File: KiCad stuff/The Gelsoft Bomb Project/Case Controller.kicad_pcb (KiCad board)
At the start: 2 copper layers, 53.3 x 55.9 mm, 9 parts, among them J1 ISP, J2 Module Connector, J3 Battery, U1 L7805, U2 ATtiny24A-PU, U3 MAX7219, U4 HDSP-B09G

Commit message: Board tweaks
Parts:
- added C1: 100uF, Capacitor_THT:CP_Radial_D6.3mm_P2.50mm, F.Cu at (120.7, 53.3)
- J3: value Battery -> Battery Header
- moved R1 8.91 mm to (135.9, 50.2)
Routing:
- net Net-(U3-Pad14): track 39.4 -> 29.6 mm, vias 0 -> 2
- net Net-(U2-Pad3): track 31.4 -> 22.1 mm, vias 0 -> 2
- net Net-(R1-Pad1): track 7.93 -> 17.1 mm, vias 0 -> 1
- net Net-(U3-Pad15): track 35.7 -> 29.0 mm, vias 0 -> 1
- net Net-(U3-Pad11): track 41.9 -> 37.1 mm, vias 0 -> 1
- net Net-(U3-Pad20): track 19.2 -> 22.9 mm
- net Net-(U3-Pad16): track 17.4 -> 20.0 mm
- net LOWPOWER: track 13.2 -> 15.5 mm
- net BUZZER: track 38.4 -> 40.3 mm
- net Net-(U3-Pad7): track 26.1 -> 27.6 mm
- net Net-(U3-Pad22): track 21.8 -> 22.9 mm
- net Net-(U3-Pad6): vias 1 -> 2
- net Earth: vias 2 -> 4
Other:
- rule trace_min: 0.2 -> 0.08

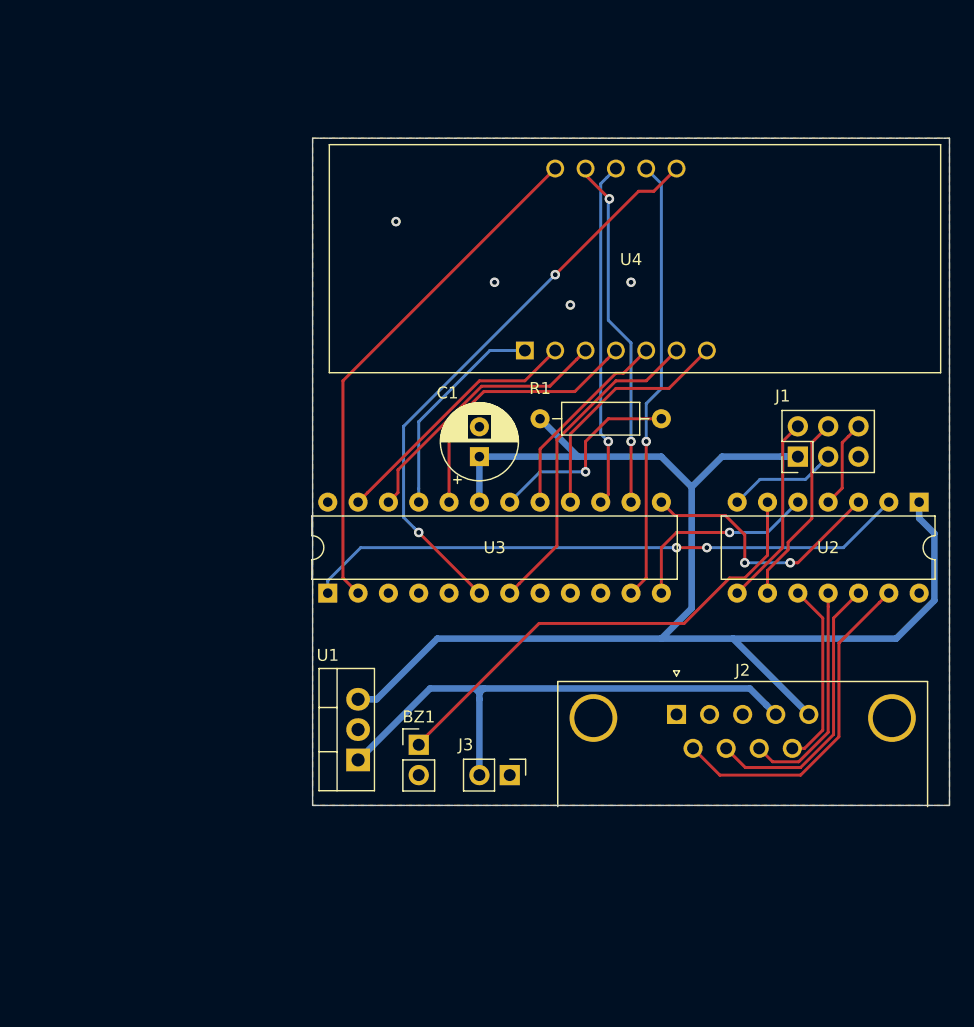
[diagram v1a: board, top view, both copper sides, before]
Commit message: Revise case controller
Added a buck converter for more efficient power regulation
Added a diode to the battery for safety
Added a power switch
Reworked the PCB design to suit these upgrades
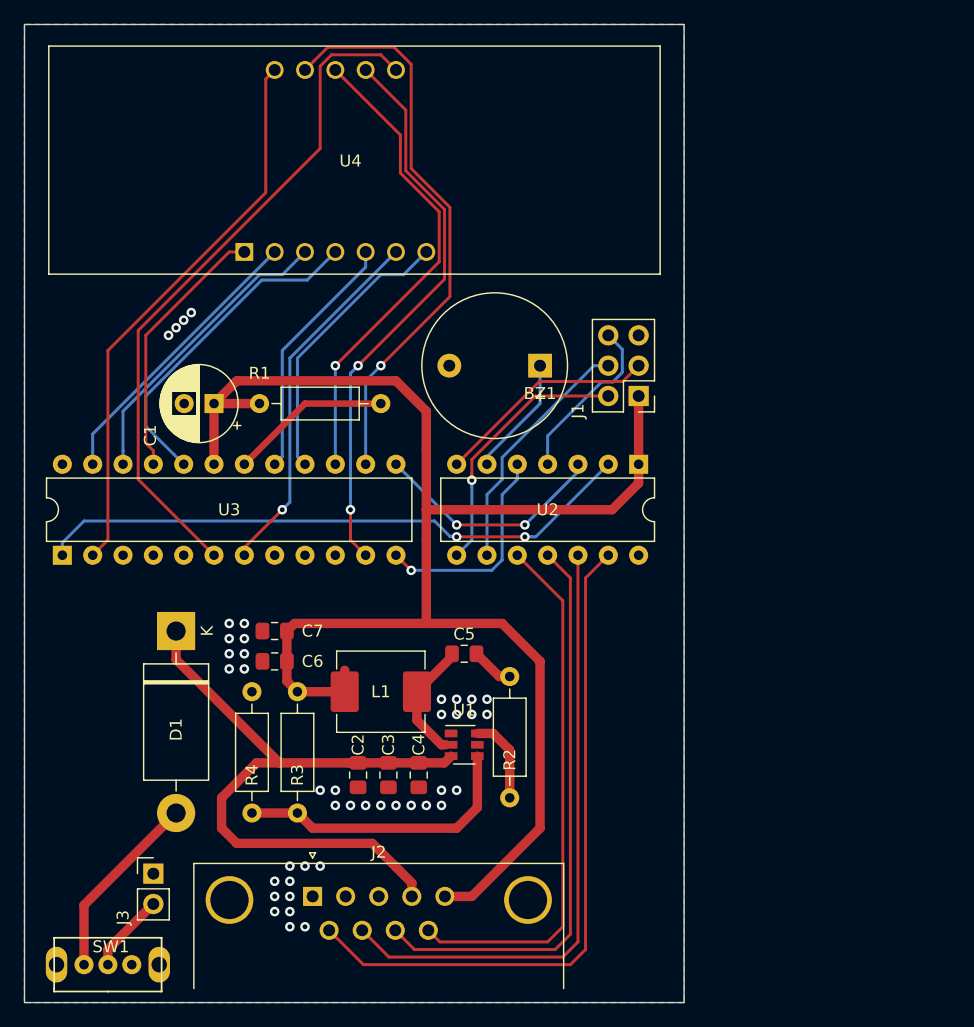
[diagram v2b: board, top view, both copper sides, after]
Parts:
- added C2: 10uF, Capacitor_SMD:C_0805_2012Metric_Pad1.15x1.40mm_HandSolder, F.Cu at (110.5, 80.0)
- added C3: 10uF, Capacitor_SMD:C_0805_2012Metric_Pad1.15x1.40mm_HandSolder, F.Cu at (113.0, 80.0)
- added C4: 0.1uF, Capacitor_SMD:C_0805_2012Metric_Pad1.15x1.40mm_HandSolder, F.Cu at (115.6, 80.0)
- added C5: 0.1uF, Capacitor_SMD:C_0805_2012Metric_Pad1.15x1.40mm_HandSolder, F.Cu at (119.4, 69.8)
- added C6: 22uF, Capacitor_SMD:C_0805_2012Metric_Pad1.15x1.40mm_HandSolder, F.Cu at (103.5, 70.5)
- added C7: 22uF, Capacitor_SMD:C_0805_2012Metric_Pad1.15x1.40mm_HandSolder, F.Cu at (103.5, 67.9)
- added D1: 1N5400, Diode_THT:D_DO-201AD_P15.24mm_Horizontal, F.Cu at (95.2, 67.9)
- added L1: 5.6uH, Inductor_SMD:L_Abracon_ASPI-0630LR, F.Cu at (112.4, 73.0)
- added R2: 30, Resistor_THT:R_Axial_DIN0207_L6.3mm_D2.5mm_P10.16mm_Horizontal, F.Cu at (123.2, 71.8)
- added R3: 52.3k, Resistor_THT:R_Axial_DIN0207_L6.3mm_D2.5mm_P10.16mm_Horizontal, F.Cu at (105.4, 73.0)
- added R4: 10k, Resistor_THT:R_Axial_DIN0207_L6.3mm_D2.5mm_P10.16mm_Horizontal, F.Cu at (101.6, 83.2)
- added SW1: Power Switch, The Gelsoft Bomb Project:SK12D07VG3, F.Cu at (89.5, 95.9)
- BZ1: footprint Connector_PinHeader_2.54mm:PinHeader_1x02_P2.54mm_Vertical -> Buzzer_Beeper:Buzzer_12x9.5RM7.6
- C1: value 100uF -> 470uF
- U1: value L7805 -> TPS56339DDCR; footprint Package_TO_SOT_THT:TO-220-3_Vertical -> Package_TO_SOT_SMD:SOT-23-6
- moved J2 34.1 mm to (106.7, 90.2)
- moved BZ1 33.3 mm to (125.7, 45.7), turned to 180 degrees
- moved J3 31.0 mm to (93.3, 88.3), turned to 0 degrees
- moved U4 24.9 mm to (103.5, 36.2)
- moved U2 23.7 mm to (134.0, 54.0)
- moved R1 23.5 mm to (112.4, 48.9)
- moved C1 22.7 mm to (98.4, 48.9), turned to 180 degrees
- moved U3 22.5 mm to (85.7, 61.6)
- moved J1 14.3 mm to (134.0, 48.3), turned to 180 degrees
- moved U1 8.98 mm to (119.4, 77.5), turned to 0 degrees
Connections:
- J3 pad 2: VIN -> Net-(J3-Pad2)
- U1 pad 1: VIN -> Earth
- U1 pad 2: Earth -> Net-(C5-Pad1)
- U1 pad 3: 5v -> VIN
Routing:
- net BUZZER: track 40.3 -> 10.1 mm
- net DISARM: track 18.9 -> 48.4 mm
- net LOWPOWER: track 15.5 -> 44.9 mm
- net CORRECT: track 28.2 -> 57.0 mm
- net STRIKE: track 23.5 -> 51.9 mm
- net Net-(R3-Pad2): track 0.00 -> 24.4 mm
- net Net-(U3-Pad14): track 29.6 -> 48.0 mm, vias 2 -> 1
- net Net-(D1-Pad2): track 0.00 -> 15.9 mm
- net Net-(U3-Pad15): track 29.0 -> 40.2 mm
- net VIN: track 46.3 -> 56.8 mm
- net Net-(C5-Pad1): track 0.00 -> 10.0 mm
- net Net-(U3-Pad11): track 37.1 -> 47.2 mm, vias 1 -> 2
- net MOSI: track 9.20 -> 18.7 mm
- net 5v: track 121.7 -> 130.6 mm
- net Net-(U3-Pad6): track 48.4 -> 57.2 mm, vias 2 -> 0
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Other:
- board size 53.3 x 55.9 mm -> 55.2 x 81.9 mm

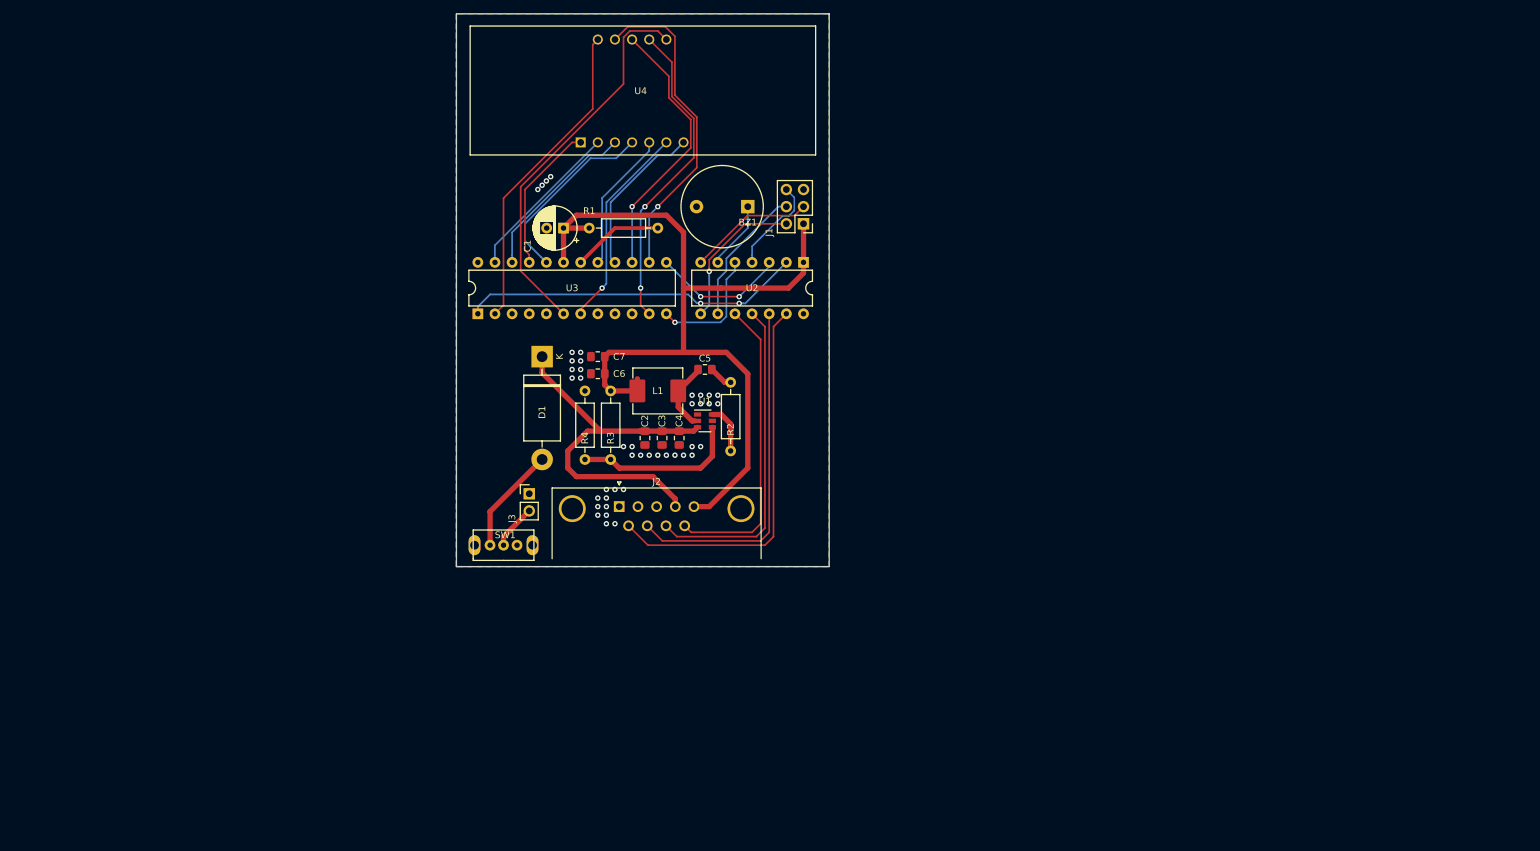
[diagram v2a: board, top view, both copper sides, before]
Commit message: Overhaul into v0.2.0 (see desc)
Added buttons to set the timer
Added the low-power switch
Added strike LEDs (2 for now, since we don't want another LED driver)
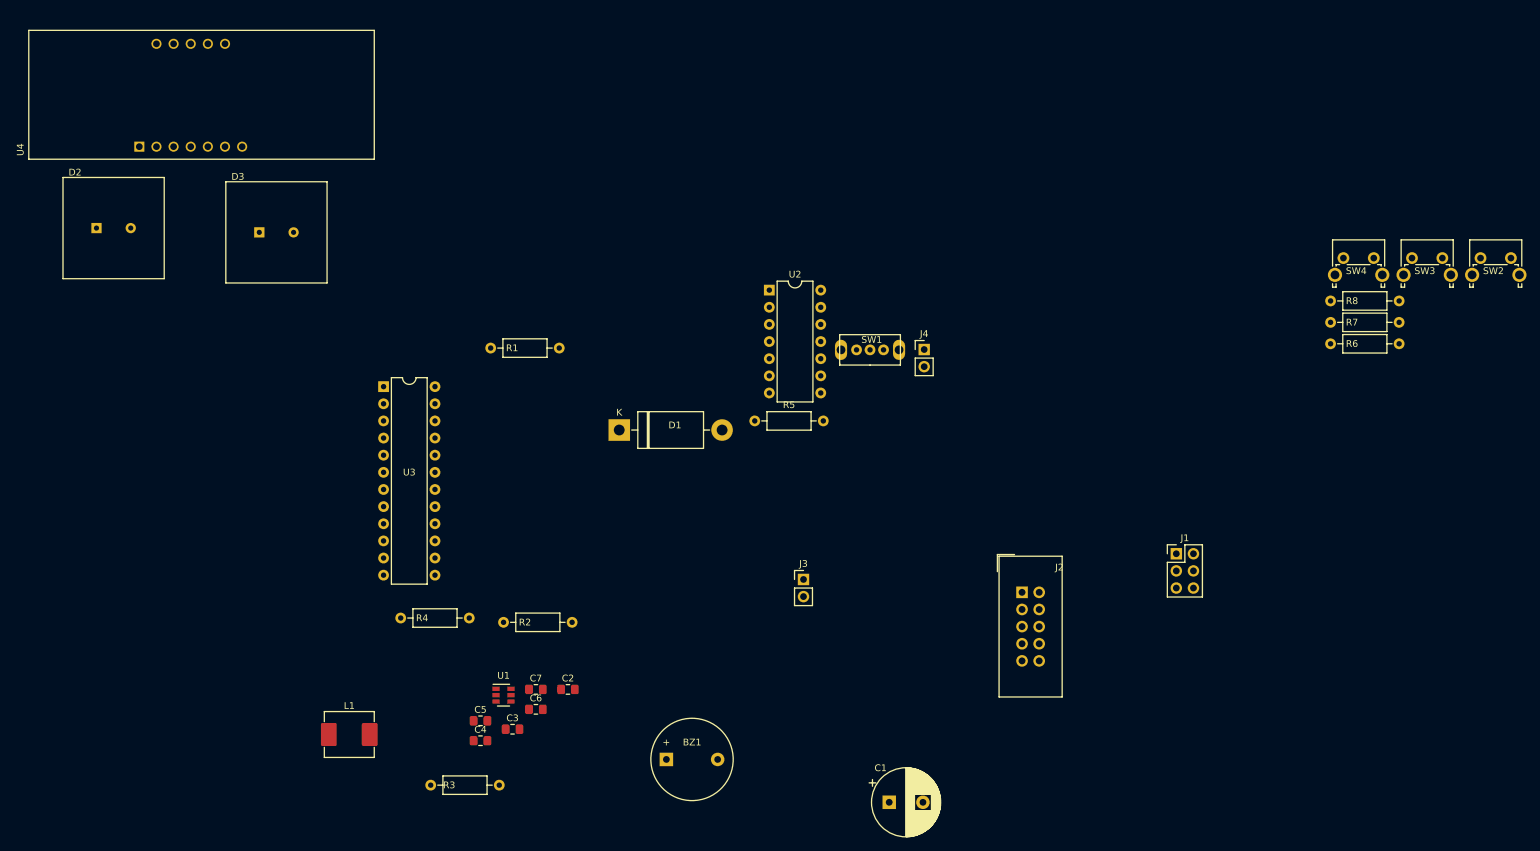
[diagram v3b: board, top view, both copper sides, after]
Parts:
- added D2: STRIKE 1, The Gelsoft Bomb Project:LED_Square_15x15mm, F.Cu at (31.8, 48.9)
- added D3: STRIKE 2, The Gelsoft Bomb Project:LED_Square_15x15mm, F.Cu at (55.9, 49.5)
- added J4: Low-Power Switch, Connector_PinHeader_2.54mm:PinHeader_1x02_P2.54mm_Vertical, F.Cu at (151.9, 66.9)
- added R5: 100k, Resistor_THT:R_Axial_DIN0207_L6.3mm_D2.5mm_P10.16mm_Horizontal, F.Cu at (126.8, 77.5)
- added R6: 100k, Resistor_THT:R_Axial_DIN0207_L6.3mm_D2.5mm_P10.16mm_Horizontal, F.Cu at (212.1, 66.0)
- added R7: 100k, Resistor_THT:R_Axial_DIN0207_L6.3mm_D2.5mm_P10.16mm_Horizontal, F.Cu at (212.1, 62.9)
- added R8: 100k, Resistor_THT:R_Axial_DIN0207_L6.3mm_D2.5mm_P10.16mm_Horizontal, F.Cu at (212.1, 59.7)
- added SW2: PLUS, Button_Switch_THT:SW_Tactile_SPST_Angled_PTS645Vx83-2LFS, F.Cu at (234.3, 53.3)
- added SW3: MINUS, Button_Switch_THT:SW_Tactile_SPST_Angled_PTS645Vx83-2LFS, F.Cu at (224.2, 53.3)
- added SW4: OK, Button_Switch_THT:SW_Tactile_SPST_Angled_PTS645Vx83-2LFS, F.Cu at (214.0, 53.3)
- C1: footprint Capacitor_THT:CP_Radial_D6.3mm_P2.50mm -> Capacitor_THT:CP_Radial_D10.0mm_P5.00mm
- J2: footprint Connector_Dsub:DSUB-9_Male_Horizontal_P2.77x2.84mm_EdgePinOffset4.94mm_Housed_MountingHolesOffset7.48mm -> Connector_IDC:IDC-Header_2x05_P2.54mm_Vertical
- moved C1 97.8 mm to (146.7, 134.0), turned to 0 degrees
- moved BZ1 82.8 mm to (113.7, 127.6), turned to 0 degrees
- moved J1 73.8 mm to (189.2, 97.2), turned to 0 degrees
- moved L1 68.4 mm to (66.7, 123.9), turned to 0 degrees
- moved U4 65.4 mm to (38.1, 36.8)
- moved R3 64.2 mm to (78.7, 131.4), turned to 0 degrees
- moved C5 61.8 mm to (86.1, 121.9)
- moved SW1 61.5 mm to (143.8, 66.9)
- moved J2 61.0 mm to (166.4, 102.9)
- moved C4 53.7 mm to (86.1, 124.9), turned to 0 degrees
- moved C6 50.6 mm to (94.3, 120.2), turned to 0 degrees
- moved U1 50.4 mm to (89.5, 118.1)
- moved C7 50.2 mm to (94.3, 117.3), turned to 0 degrees
- moved R2 49.0 mm to (89.5, 107.3), turned to 0 degrees
- moved C3 48.5 mm to (90.9, 123.2), turned to 0 degrees
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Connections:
- J2 pad 2: Net-(J2-Pad2) -> Earth
- J2 pad 3: Net-(J2-Pad3) -> MOSI
- J2 pad 4: VIN -> MISO
- J2 pad 5: 5v -> SCK
- J2 pad 6: CORRECT -> Earth
- J2 pad 7: STRIKE -> Earth
- J2 pad 8: DISARM -> VIN
- J2 pad 9: LOWPOWER -> 5v
- U2 pad 10: LOWPOWER -> OK
- U2 pad 11: DISARM -> MINUS
- U2 pad 12: STRIKE -> PLUS
- U2 pad 13: CORRECT -> LOWPOWER
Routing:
- net 5v: track 130.6 -> 0.00 mm
- net Net-(U3-Pad6): track 57.2 -> 0.00 mm
- net CORRECT: track 57.0 -> 0.00 mm
- net VIN: track 56.8 -> 0.00 mm
- net STRIKE: track 51.9 -> 0.00 mm
- net Net-(U2-Pad2): track 50.6 -> 0.00 mm, vias 2 -> 0
- net DISARM: track 48.4 -> 0.00 mm
- net Net-(U3-Pad14): track 48.0 -> 0.00 mm, vias 1 -> 0
- net Net-(U3-Pad11): track 47.2 -> 0.00 mm, vias 2 -> 0
- net Net-(D2-Pad1): track 47.0 -> 0.00 mm
- net LOWPOWER: track 44.9 -> 0.00 mm
- net Net-(U3-Pad15): track 40.2 -> 0.00 mm, vias 1 -> 0
- net Net-(D3-Pad1): track 30.7 -> 0.00 mm, vias 1 -> 0
- net Net-(U3-Pad20): track 27.9 -> 0.00 mm
- net Net-(D2-Pad2): track 25.2 -> 0.00 mm
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- removed copper zone on B.Cu, net Earth
- removed copper zone on F.Cu, net Earth
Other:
- board outline removed

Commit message: Replace buck converter with a pre-made module
Bugger having to deal with making my own, we'll just keep things simple and cheap
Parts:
- added U1: Buck_Converter_Module_7-26v, The Gelsoft Bomb Project:Buck_Converter_Module_7-24v, F.Cu at (151.1, 31.8)
- moved U3 42.1 mm to (75.6, 30.5)
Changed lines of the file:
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@@
     (tracks 0)
     (zones 0)
-    (modules 32)
+    (modules 33)
     (nets 45)
   )
@@
     (add_net VIN)
   )
+  (module "The Gelsoft Bomb Project:Buck_Converter_Module_7-24v" (layer F.Cu)
+    (at 151.13 31.75)
+    (fp_text reference U1 (at 2 -1) (layer F.SilkS)
+      (effects (font (size 1 1) (thickness 0.15)))
+    )
+    (fp_text value Buck_Converter_Module_7-26v (at 11 19) (layer F.Fab)
+      (effects (font (size 1 1) (thickness 0.15)))
+    )
+    (fp_text user "Vin -" (at 1.27 11.43) (layer F.SilkS)
+      (effects (font (size 1 1) (thickness 0.15)) (justify left))
+    )
+    (fp_text user "Vin +" (at 1.27 6.985) (layer F.SilkS)
+      (effects (font (size 1 1) (thickness 0.15)) (justify left))
+    )
+    (fp_text user "Vout -" (at 20.955 11.43) (layer F.SilkS)
+      (effects (font (size 1 1) (thickness 0.15)) (justify right))
+    )
+    (fp_text user "Vout +" (at 20.955 6.985) (layer F.SilkS)
+      (effects (font (size 1 1) (thickness 0.15)) (justify right))
+    )
+    (fp_line (start 0 0) (end 0 17.8) (layer F.SilkS) (width 0.12))
+    (fp_line (start 22 17.8) (end 22 0) (layer F.SilkS) (width 0.12))
+    (fp_line (start 0 17.8) (end 22 17.8) (layer F.SilkS) (width 0.12))
+    (fp_line (start 0 0) (end 22 0) (layer F.SilkS) (width 0.12))
+    (pad 4 smd custom (at 22 13.04) (size 1.5 1.5) (layers F.Cu F.Paste F.Mask)
+      (net 1 Earth) (zone_connect 0)
+      (options (clearance outline) (anchor circle))
+      (primitives
+        (gr_poly (pts
+           (xy -0.75 -0.75) (xy 0.75 -0.75) (xy 0.75 0.75) (xy -0.75 0.75)) (width 0))
+        (gr_circle (center 0.75 0) (end 0.75 0) (width 1.5))
+        (gr_circle (center -0.75 0) (end -0.75 0) (width 1.5))
+      ))
+    (pad 4 smd custom (at 22 15.58) (size 1.5 1.5) (layers F.Cu F.Paste F.Mask)
+      (net 1 Earth) (zone_connect 0)
+      (options (clearance outline) (anchor circle))
+      (primitives
+        (gr_poly (pts
+           (xy -0.75 -0.75) (xy 0.75 -0.75) (xy 0.75 0.75) (xy -0.75 0.75)) (width 0))
+        (gr_circle (center 0.75 0) (end 0.75 0) (width 1.5))
+        (gr_circle (center -0.75 0) (end -0.75 0) (width 1.5))
+      ))
+    (pad 3 smd custom (at 22 5.04) (size 1.5 1.5) (layers F.Cu F.Paste F.Mask)
+      (net 7 5v) (zone_connect 0)
+      (options (clearance outline) (anchor circle))
+      (primitives
+        (gr_poly (pts
+           (xy -0.75 -0.75) (xy 0.75 -0.75) (xy 0.75 0.75) (xy -0.75 0.75)) (width 0))
+        (gr_circle (center 0.75 0) (end 0.75 0) (width 1.5))
+        (gr_circle (center -0.75 0) (end -0.75 0) (width 1.5))
+      ))
+    (pad 3 smd custom (at 22 2.5) (size 1.5 1.5) (layers F.Cu F.Paste F.Mask)
+      (net 7 5v) (zone_connect 0)
+      (options (clearance outline) (anchor circle))
+      (primitives
+        (gr_poly (pts
+           (xy -0.75 -0.75) (xy 0.75 -0.75) (xy 0.75 0.75) (xy -0.75 0.75)) (width 0))
+        (gr_circle (center 0.75 0) (end 0.75 0) (width 1.5))
+        (gr_circle (center -0.75 0) (end -0.75 0) (width 1.5))
+      ))
+    (pad 2 smd custom (at 0 13.04) (size 1.5 1.5) (layers F.Cu F.Paste F.Mask)
+      (net 1 Earth) (zone_connect 0)
+      (options (clearance outline) (anchor circle))
+      (primitives
+        (gr_poly (pts
+           (xy -0.75 -0.75) (xy 0.75 -0.75) (xy 0.75 0.75) (xy -0.75 0.75)) (width 0))
+        (gr_circle (center 0.75 0) (end 0.75 0) (width 1.5))
+        (gr_circle (center -0.75 0) (end -0.75 0) (width 1.5))
+      ))
+    (pad 2 smd custom (at 0 15.58) (size 1.5 1.5) (layers F.Cu F.Paste F.Mask)
+      (net 1 Earth) (zone_connect 0)
+      (options (clearance outline) (anchor circle))
+      (primitives
+        (gr_poly (pts
+           (xy -0.75 -0.75) (xy 0.75 -0.75) (xy 0.75 0.75) (xy -0.75 0.75)) (width 0))
+        (gr_circle (center 0.75 0) (end 0.75 0) (width 1.5))
+        (gr_circle (center -0.75 0) (end -0.75 0) (width 1.5))
+      ))
+    (pad 1 smd custom (at 0 5.04) (size 1.5 1.5) (layers F.Cu F.Paste F.Mask)
+      (net 9 VIN) (zone_connect 0)
+      (options (clearance outline) (anchor circle))
+      (primitives
+        (gr_poly (pts
+           (xy -0.75 -0.75) (xy 0.75 -0.75) (xy 0.75 0.75) (xy -0.75 0.75)) (width 0))
+        (gr_circle (center 0.75 0) (end 0.75 0) (width 1.5))
+        (gr_circle (center -0.75 0) (end -0.75 0) (width 1.5))
+      ))
+    (pad 1 smd custom (at 0 2.5) (size 1.5 1.5) (layers F.Cu F.Paste F.Mask)
+      (net 9 VIN)
+      (options (clearance outline) (anchor circle))
+      (primitives
+        (gr_poly (pts
+           (xy -0.75 -0.75) (xy 0.75 -0.75) (xy 0.75 0.75) (xy -0.75 0.75)) (width 0))
+        (gr_circle (center 0.75 0) (end 0.75 0) (width 1.5))
+        (gr_circle (center -0.75 0) (end -0.75 0) (width 1.5))
+      ))
+  )
   (module "The Gelsoft Bomb Project:LED_Square_15x15mm" (layer F.Cu)
     (at 55.88 49.53)
@@
   )
   (module Package_DIP:DIP-24_W7.62mm (layer F.Cu)
-    (at 71.755 72.39)
+    (at 75.565 30.48)
     (descr "24-lead though-hole mounted DIP package, row spacing 7.62 mm (300 mils)")
     (tags "THT DIP DIL PDIP 2.54mm 7.62mm 300mil")
